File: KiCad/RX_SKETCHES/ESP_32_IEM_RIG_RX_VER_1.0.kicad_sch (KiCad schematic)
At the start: 0 parts

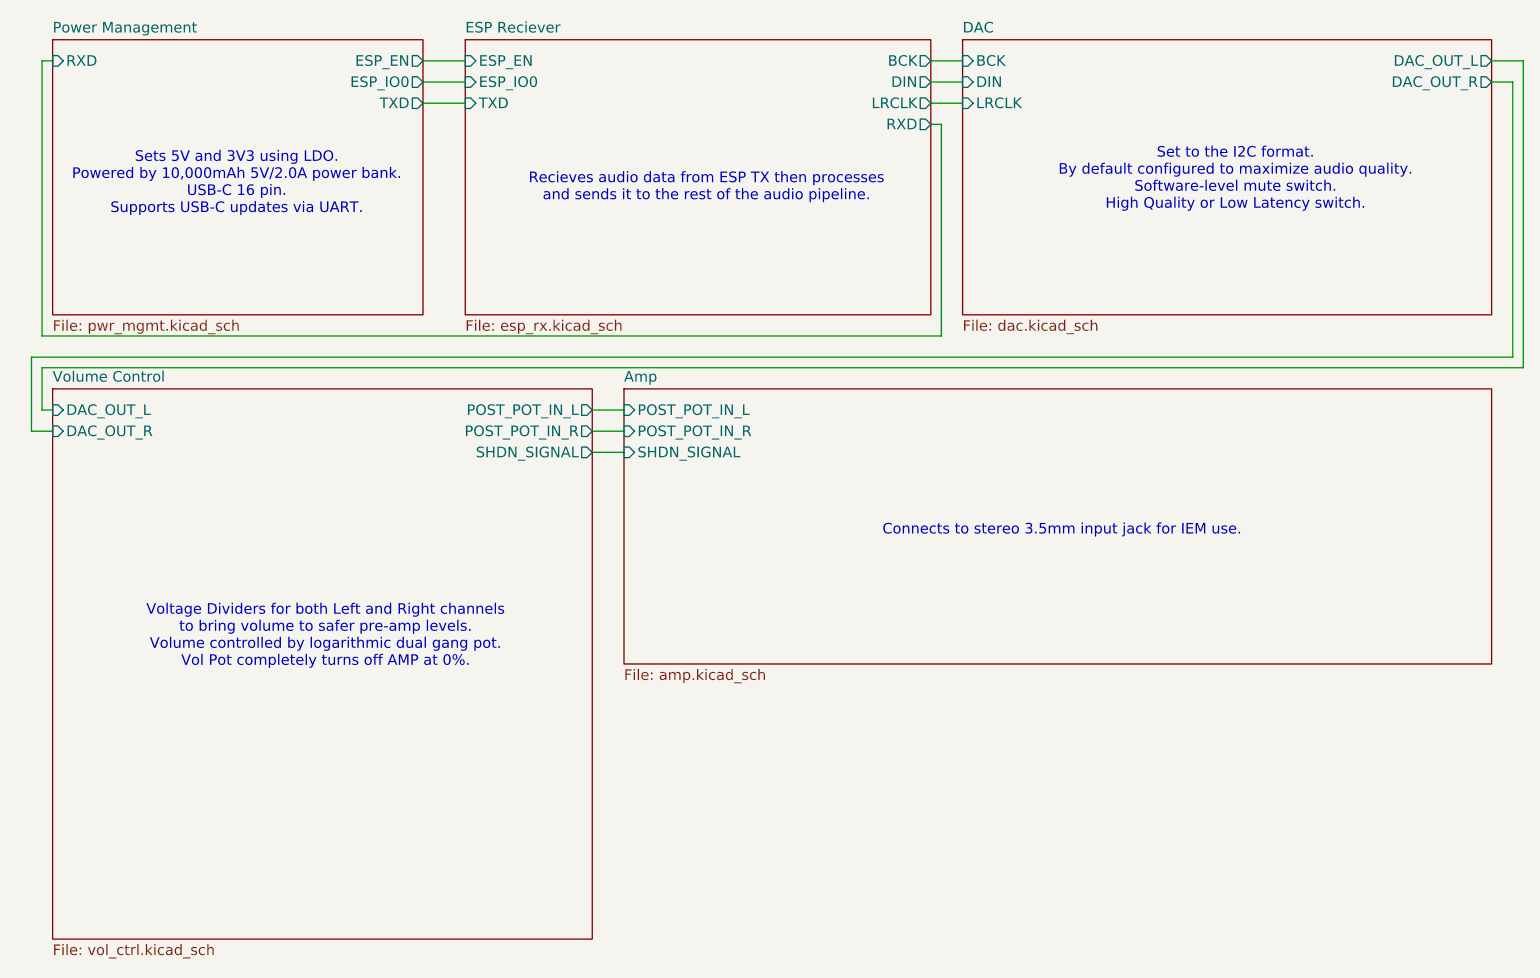
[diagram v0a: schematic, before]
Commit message: RX v1: complete PCB layout, retune analog chain, fix ESD clamp placement
Brings the RX schematic and board up to a fabricable state. DRC is clean:
zero unconnected items, zero schematic-parity issues. The 16 remaining
violations are footprint-inherent and documented rather than worked around
(ESP32-WROOM thermal via array drilled 0.2 mm against a 0.3 mm rule, and
USB-C NPTH-to-pad spacing from the vendor land pattern).

Analog:
- Gain network populated at RF 4.7k / RIN 47k (-20 dB) rather than DNP 10k.
  Tames the PCM5102's 2.1 Vrms into sensitive IEMs, gives the 10k pot a
  4.7x loading ratio instead of 1:1, and lifts the coupling corner clear of
  the audible band.
- Coupling caps C1-C4 raised 0.47uF -> 1uF. Corner 7.2 Hz -> 3.4 Hz, and it
  halves the signal developed across the ceramic at 20 Hz, which is where
  Class-II dielectric distortion actually shows up.
- PCM5102 mode pins no longer float: 100k pulldowns on FLT and XSMT, with
  DEMP and FMT strapped to GND.

Power and protection:
- D1's third TVS channel moved off the switched +5V rail onto VBUS_RAW. An
  ESD clamp has to sit on the connector pin exposed to a finger; behind the
  power switch it disconnected exactly when the board is most likely to be
  handled. The off state is unaffected -- a TVS is open below its standoff
  voltage and SW4 still breaks the rail.
- All three slide switches now follow one rule: the open throw is the safe
  default (powered off / normal-latency filter / muted).

Housekeeping:
- C28 and mounting holes REF1-REF4 added to the schematic, clearing parity
  errors against parts that previously existed only on the PCB.
- Gain, loudness, and filter math written up in README.org with sources so
  the numbers can be re-derived; rationale logged in hardware_revisions.org.
- .gitignore now covers the editor .history/ directory and ESP-IDF build
  output, which were showing up as untracked noise.

Firmware and build artifacts are deliberately excluded from this commit.

Co-authored-b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
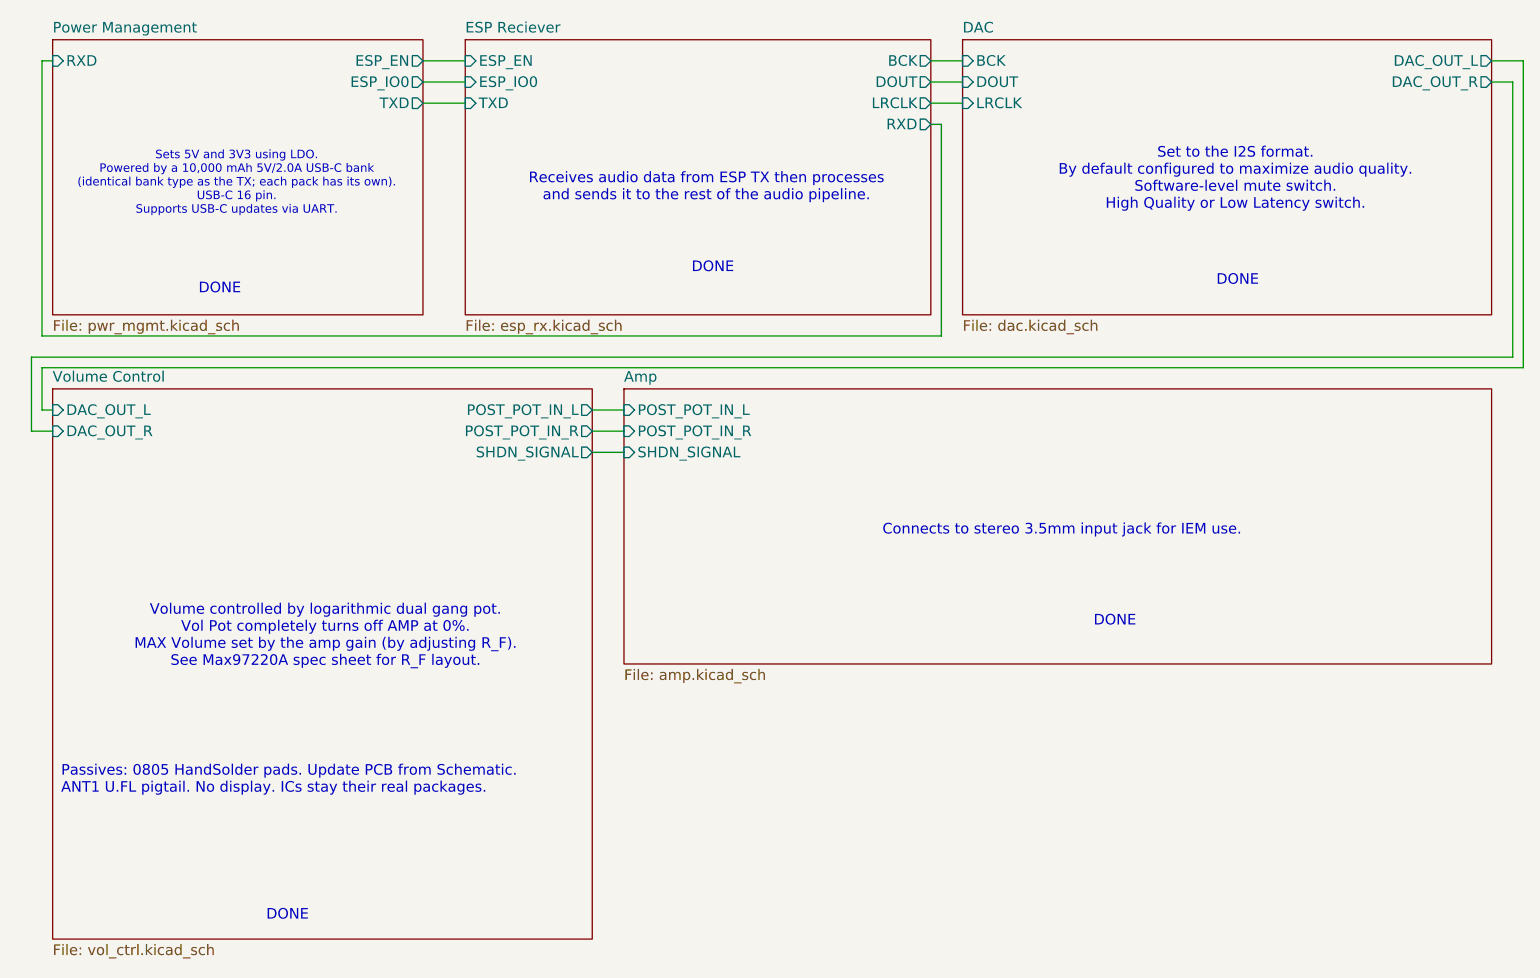
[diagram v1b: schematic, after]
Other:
- sheet DAC ports: added DOUT; removed DIN
- sheet ESP Reciever ports: added DOUT; removed DIN
- note added: "DONE"
- note added: "Passives: 0805 HandSolder pads. Update PCB from Schematic. ANT1 U.FL pigtail. No display. ICs stay their real packages."
- note added: "Receives audio data from ESP TX then processes and sends it to the rest of the audio pipeline."
- note added: "Set to the I2S format. By default configured to maximize audio quality. Software-level mute switch. High Quality or Low Latency switch."
- note added: "Sets 5V and 3V3 using LDO. Powered by a 10,000 mAh 5V/2.0A USB-C bank (identical bank type as the TX; each pack has its own). USB-C 16 pin. Supports USB-C updates via UART."
- note added: "Volume controlled by logarithmic dual gang pot. Vol Pot completely turns off AMP at 0%. MAX Volume set by the amp gain (by adjusting R_F). See Max97220A spec sheet for R_F layout."
- note removed: "Recieves audio data from ESP TX then processes and sends it to the rest of the audio pipeline."
- note removed: "Set to the I2C format. By default configured to maximize audio quality. Software-level mute switch. High Quality or Low Latency switch."
- note removed: "Sets 5V and 3V3 using LDO. Powered by 10,000mAh 5V/2.0A power bank. USB-C 16 pin. Supports USB-C updates via UART."
- note removed: "Voltage Dividers for both Left and Right channels to bring volume to safer pre-amp levels. Volume controlled by logarithmic dual gang pot. Vol Pot completely turns off AMP at 0%."
- title: ESP32 Wireless IEM Rig Reciever -> ESP32U- WROOM Wireless IEM Rig Reciever
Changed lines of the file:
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@@
 	(paper "A5")
 	(title_block
-		(title "ESP32 Wireless IEM Rig Reciever")
+		(title "ESP32U- WROOM Wireless IEM Rig Reciever")
 		(date "2026-08-04")
 		(rev "1.0.0")
@@
 		(comment 4 "Supports updates over USB-C using UART.")
 	)
-	(text "Voltage Dividers for both Left and Right channels\nto bring volume to safer pre-amp levels. \nVolume controlled by logarithmic dual gang pot.\nVol Pot completely turns off AMP at 0%.\n"
+	(text "DONE"
+		(exclude_from_sim no)
+		(at 37.846 51.562 0)
+		(effects
+			(font
+				(size 1.27 1.27)
+			)
+		)
+	)
+	(text "DONE"
+		(exclude_from_sim no)
+		(at 97.028 49.022 0)
+		(effects
+			(font
+				(size 1.27 1.27)
+			)
+		)
+	)
+	(text "Volume controlled by logarithmic dual gang pot.\nVol Pot completely turns off AMP at 0%.\nMAX Volume set by the amp gain (by adjusting R_F). \nSee Max97220A spec sheet for R_F layout."
 		(exclude_from_sim no)
 		(at 50.546 93.218 0)
@@
 		)
 	)
-	(text "Recieves audio data from ESP TX then processes \nand sends it to the rest of the audio pipeline."
+	(text "DONE"
+		(exclude_from_sim no)
+		(at 160.02 50.546 0)
+		(effects
+			(font
+				(size 1.27 1.27)
+			)
+		)
+	)
+	(text "DONE"
+		(exclude_from_sim no)
+		(at 145.288 91.44 0)
+		(effects
+			(font
+				(size 1.27 1.27)
+			)
+		)
+	)
+	(text "DONE"
+		(exclude_from_sim no)
+		(at 45.974 126.746 0)
+		(effects
+			(font
+				(size 1.27 1.27)
+			)
+		)
+	)
+	(text "Receives audio data from ESP TX then processes \nand sends it to the rest of the audio pipeline."
 		(exclude_from_sim no)
 		(at 96.266 39.37 0)
@@
 		)
 	)
-	(text "Sets 5V and 3V3 using LDO. \nPowered by 10,000mAh 5V/2.0A power bank.\nUSB-C 16 pin. \nSupports USB-C updates via UART."
+	(text "Passives: 0805 HandSolder pads. Update PCB from Schematic.\nANT1 U.FL pigtail. No display. ICs stay their real packages."
+		(exclude_from_sim no)
+		(at 18.796 110.49 0)
+		(effects
+			(font
+				(size 1.27 1.27)
+			)
+			(justify left)
+		)
+	)
+	(text "Sets 5V and 3V3 using LDO.\nPowered by a 10,000 mAh 5V/2.0A USB-C bank\n(identical bank type as the TX; each pack has its own).\nUSB-C 16 pin. \nSupports USB-C updates via UART."
 		(exclude_from_sim no)
 		(at 39.878 38.862 0)
 		(effects
 			(font
-				(size 1.27 1.27)
-			)
-		)
-	)
-	(text "Set to the I2C format. \nBy default configured to maximize audio quality.\nSoftware-level mute switch.\nHigh Quality or Low Latency switch."
+				(size 1.016 1.016)
+			)
+		)
+	)
+	(text "Set to the I2S format. \nBy default configured to maximize audio quality.\nSoftware-level mute switch.\nHigh Quality or Low Latency switch."
 		(exclude_from_sim no)
 		(at 159.766 38.354 0)
@@
 	(wire
 		(pts
+			(xy 123.19 26.67) (xy 127 26.67)
+		)
+		(stroke
+			(width 0)
+			(type default)
+		)
+	)
+	(wire
+		(pts
 			(xy 15.24 59.69) (xy 15.24 68.58)
 		)
@@
 		(pts
 			(xy 62.23 24.13) (xy 67.31 24.13)
-		)
-		(stroke
-			(width 0)
-			(type default)
-		)
-	)
-	(wire
-		(pts
-			(xy 123.19 26.67) (xy 127 26.67)
 		)
 		(stroke
@@
 			)
 		)
-		(pin "DIN" output
-			(at 123.19 26.67 0)
-			(effects
-				(font
-					(size 1.27 1.27)
-				)
-				(justify right)
-			)
-		)
 		(pin "LRCLK" output
 			(at 123.19 29.21 0)
@@
 		(pin "RXD" output
 			(at 123.19 31.75 0)
+			(effects
+				(font
+					(size 1.27 1.27)
+				)
+				(justify right)
+			)
+		)
+		(pin "DOUT" output
+			(at 123.19 26.67 0)
 			(effects
 				(font
@@
 			)
 		)
-		(pin "DIN" input
-			(at 127 26.67 180)
-			(effects
-				(font
-					(size 1.27 1.27)
-				)
-				(justify left)
-			)
-		)
 		(pin "LRCLK" input
 			(at 127 29.21 180)
@@
 			)
 		)
+		(pin "DOUT" input
+			(at 127 26.67 180)
+			(effects
+				(font
+					(size 1.27 1.27)
+				)
+				(justify left)
+			)
+		)
